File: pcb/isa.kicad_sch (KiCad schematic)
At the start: 9 parts, among them J1 Bus_ISA_16bit, J2 Bus_ISA_16bit

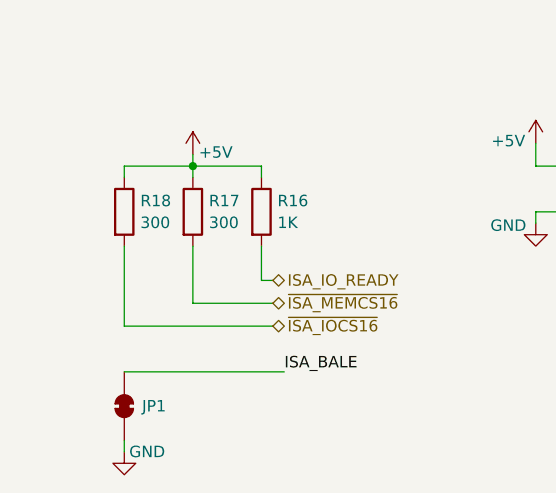
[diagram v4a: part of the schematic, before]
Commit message: ISA BALE multiple optios for wiring to ground/Vcc/custom
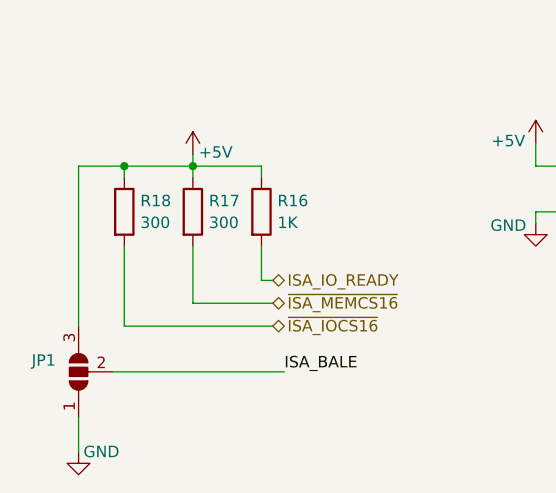
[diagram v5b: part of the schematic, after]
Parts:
- removed JP1: SolderJumper_2_Bridged, Jumper:SolderJumper-2_P1.3mm_Bridged_RoundedPad1.0x1.5mm, symbol Jumper:SolderJumper_2_Bridged
- added JP1: BALE, Jumper:SolderJumper-3_P2.0mm_Open_TrianglePad1.0x1.5mm, symbol Jumper:SolderJumper_3_Open
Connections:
- net +5V: now also JP1.3 (B)
- net GND: now also JP1.1 (A)
- net ISA_BALE: now also JP1.2 (C)
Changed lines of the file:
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@@
 		(color 0 0 0 0)
 	)
+	(junction
+		(at 35.56 149.86)
+		(diameter 0)
+		(color 0 0 0 0)
+	)
 	(no_connect
 		(at 144.78 134.62)
@@
 	(wire
 		(pts
-			(xy 35.56 180.34) (xy 35.56 181.61)
-		)
-		(stroke
-			(width 0)
-			(type default)
-		)
-	)
-	(wire
-		(pts
 			(xy 81.28 53.34) (xy 104.14 53.34)
 		)
@@
 	(wire
 		(pts
+			(xy 30.48 177.8) (xy 30.48 181.61)
+		)
+		(stroke
+			(width 0)
+			(type default)
+		)
+	)
+	(wire
+		(pts
 			(xy 58.42 44.45) (xy 58.42 45.72)
 		)
@@
 	(wire
 		(pts
+			(xy 35.56 149.86) (xy 43.18 149.86)
+		)
+		(stroke
+			(width 0)
+			(type default)
+		)
+	)
+	(wire
+		(pts
 			(xy 100.33 33.02) (xy 104.14 33.02)
 		)
@@
 	(wire
 		(pts
-			(xy 35.56 172.72) (xy 53.34 172.72)
-		)
-		(stroke
-			(width 0)
-			(type default)
-		)
-	)
-	(wire
-		(pts
 			(xy 144.78 91.44) (xy 149.86 91.44)
 		)
@@
 		)
 	)
+	(wire
+		(pts
+			(xy 30.48 149.86) (xy 30.48 167.64)
+		)
+		(stroke
+			(width 0)
+			(type default)
+		)
+	)
 	(bus
 		(pts
@@
 	(wire
 		(pts
+			(xy 34.29 172.72) (xy 53.34 172.72)
+		)
+		(stroke
+			(width 0)
+			(type default)
+		)
+	)
+	(wire
+		(pts
 			(xy 201.93 83.82) (xy 205.74 83.82)
 		)
@@
 	(wire
 		(pts
+			(xy 30.48 149.86) (xy 35.56 149.86)
+		)
+		(stroke
+			(width 0)
+			(type default)
+		)
+	)
+	(wire
+		(pts
 			(xy 246.38 106.68) (xy 251.46 106.68)
 		)
@@
 	(wire
 		(pts
-			(xy 35.56 149.86) (xy 43.18 149.86)
-		)
-		(stroke
-			(width 0)
-			(type default)
-		)
-	)
-	(wire
-		(pts
 			(xy 246.38 127) (xy 251.46 127)
 		)
@@
 	)
 	(symbol
-		(lib_id "Jumper:SolderJumper_2_Bridged")
-		(at 35.56 176.53 90)
+		(lib_id "power:GND")
+		(at 30.48 181.61 0)
 		(unit 1)
 		(exclude_from_sim no)
-		(in_bom no)
+		(in_bom yes)
 		(on_board yes)
 		(dnp no)
-		(property "Reference" "JP1"
-			(at 38.862 176.53 90)
+		(property "Reference" "#PWR0105"
+			(at 30.48 187.96 0)
 			(effects
 				(font
 					(size 1.27 1.27)
 				)
+				(hide yes)
 			)
 		)
-		(property "Value" "SolderJumper_2_Bridged"
-			(at 31.75 176.53 0)
+		(property "Value" "GND"
+			(at 33.02 181.61 0)
 			(effects
 				(font
 					(size 1.27 1.27)
 				)
-				(hide yes)
 			)
 		)
-		(property "Footprint" "Jumper:SolderJumper-2_P1.3mm_Bridged_RoundedPad1.0x1.5mm"
-			(at 35.56 176.53 0)
+		(property "Footprint" ""
+			(at 30.48 181.61 0)
 			(effects
 				(font
@@
 			)
 		)
-		(property "Datasheet" "~"
-			(at 35.56 176.53 0)
+		(property "Datasheet" ""
+			(at 30.48 181.61 0)
 			(effects
 				(font
@@
 			)
 		)
-		(property "Description" "Solder Jumper, 2-pole, closed/bridged"
-			(at 35.56 176.53 0)
+		(property "Description" "Power symbol creates a global label with name \"GND\" , ground"
+			(at 30.48 181.61 0)
 			(effects
 				(font
@@
 		(pin "1"
 		)
-		(pin "2"
-		)
 		(instances
 			(project "homebrew_486"
 				(path "/360fb3b9-a21a-4226-8954-bf45cf17bb35/8c5c6d69-b749-4a24-8458-c5389575129e"
-					(reference "JP1")
+					(reference "#PWR0105")
 					(unit 1)
 				)
@@
 	(symbol
 		(lib_id "power:GND")
-		(at 35.56 181.61 0)
+		(at 33.02 45.72 0)
 		(unit 1)
 		(exclude_from_sim no)
@@
 		(on_board yes)
 		(dnp no)
-		(property "Reference" "#PWR0105"
-			(at 35.56 187.96 0)
+		(property "Reference" "#PWR0136"
+			(at 33.02 52.07 0)
 			(effects
 				(font
@@
 		)
 		(property "Value" "GND"
-			(at 38.1 181.61 0)
+			(at 36.068 45.466 0)
 			(effects
 				(font
@@
 		)
 		(property "Footprint" ""
-			(at 35.56 181.61 0)
+			(at 33.02 45.72 0)
 			(effects
 				(font
@@
 		)
 		(property "Datasheet" ""
-			(at 35.56 181.61 0)
+			(at 33.02 45.72 0)
 			(effects
 				(font
@@
 		)
 		(property "Description" "Power symbol creates a global label with name \"GND\" , ground"
-			(at 35.56 181.61 0)
+			(at 33.02 45.72 0)
 			(effects
 				(font
@@
 			(project "homebrew_486"
 				(path "/360fb3b9-a21a-4226-8954-bf45cf17bb35/8c5c6d69-b749-4a24-8458-c5389575129e"
-					(reference "#PWR0105")
+					(reference "#PWR0136")
 					(unit 1)
 				)
@@
 	)
 	(symbol
-		(lib_id "power:GND")
-		(at 33.02 45.72 0)
+		(lib_id "Jumper:SolderJumper_3_Open")
+		(at 30.48 172.72 90)
 		(unit 1)
 		(exclude_from_sim no)
-		(in_bom yes)
+		(in_bom no)
 		(on_board yes)
 		(dnp no)
-		(property "Reference" "#PWR0136"
-			(at 33.02 52.07 0)
+		(fields_autoplaced yes)
+		(property "Reference" "JP1"
+			(at 27.94 171.4499 90)
 			(effects
 				(font
 					(size 1.27 1.27)
 				)
-				(hide yes)
+				(justify left)
 			)
 		)
-		(property "Value" "GND"
-			(at 36.068 45.466 0)
+		(property "Value" "BALE"
+			(at 27.94 173.9899 90)
 			(effects
 				(font
 					(size 1.27 1.27)
 				)
+				(justify left)
+				(hide yes)
 			)
 		)
-		(property "Footprint" ""
-			(at 33.02 45.72 0)
+		(property "Footprint" "Jumper:SolderJumper-3_P2.0mm_Open_TrianglePad1.0x1.5mm"
+			(at 30.48 172.72 0)
 			(effects
 				(font
@@
 			)
 		)
-		(property "Datasheet" ""
-			(at 33.02 45.72 0)
+		(property "Datasheet" "~"
+			(at 30.48 172.72 0)
 			(effects
 				(font
@@
 			)
 		)
-		(property "Description" "Power symbol creates a global label with name \"GND\" , ground"
-			(at 33.02 45.72 0)
+		(property "Description" "Solder Jumper, 3-pole, open"
+			(at 30.48 172.72 0)
 			(effects
 				(font
@@
 		(pin "1"
 		)
+		(pin "3"
+		)
+		(pin "2"
+		)
 		(instances
-			(project "homebrew_486"
+			(project ""
 				(path "/360fb3b9-a21a-4226-8954-bf45cf17bb35/8c5c6d69-b749-4a24-8458-c5389575129e"
-					(reference "#PWR0136")
+					(reference "JP1")
 					(unit 1)
 				)

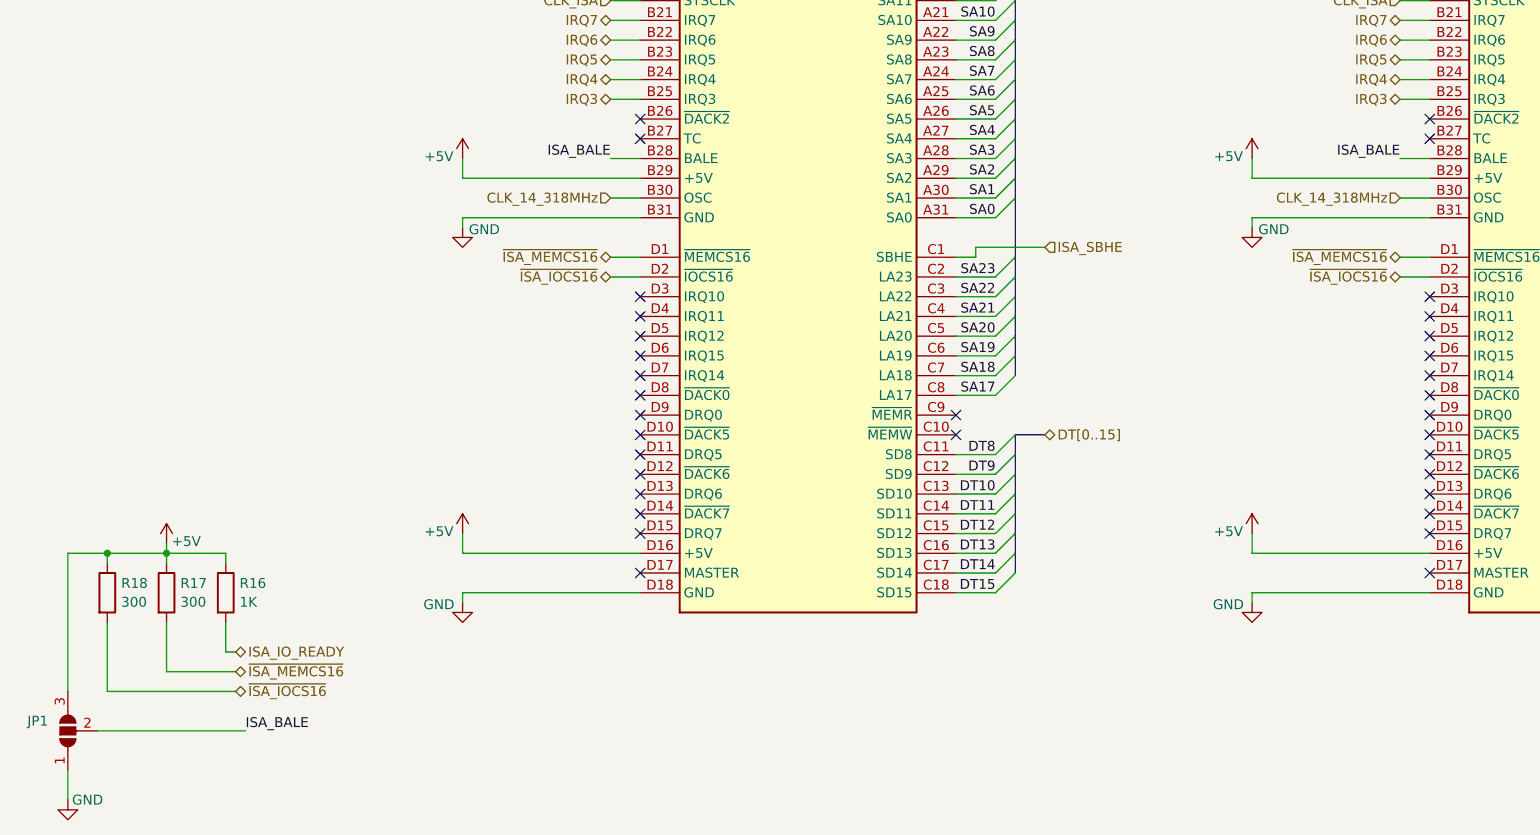
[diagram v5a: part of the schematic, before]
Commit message: handle ISA_BALE by FPGA
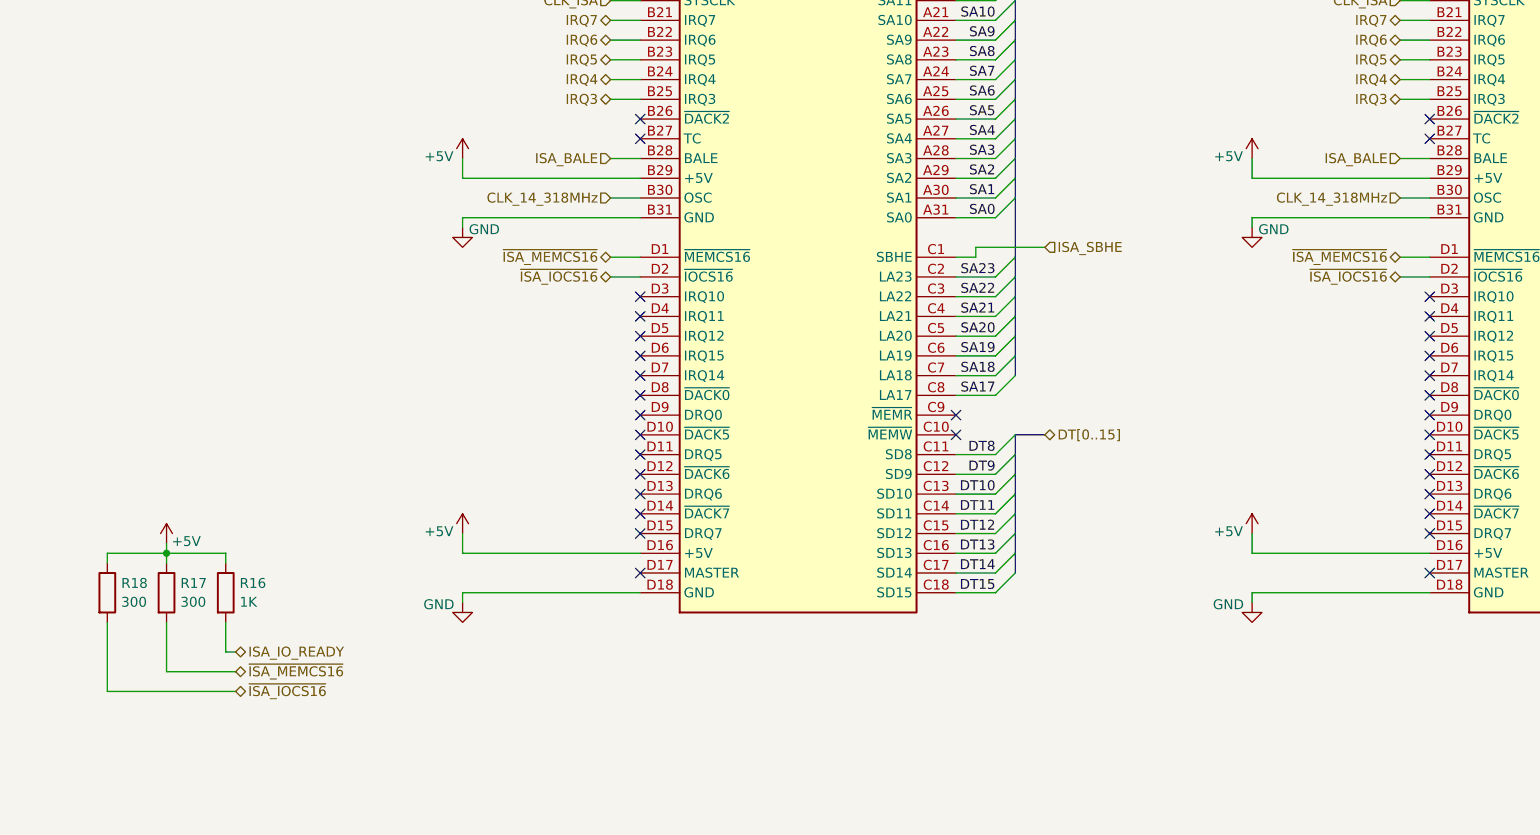
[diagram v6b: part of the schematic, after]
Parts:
- removed JP1: BALE, Jumper:SolderJumper-3_P2.0mm_Open_TrianglePad1.0x1.5mm, symbol Jumper:SolderJumper_3_Open
